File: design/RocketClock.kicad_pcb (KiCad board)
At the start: 2 copper layers, 100 x 100 mm, 98 parts, among them P1 USB_C_Plug_USB2.0, Q1 SS8050, Q2 SS8050, SW1 SW_MEC_5E, U1 TLV75533PDBV, U2 MAX7219, U3 TMP112xxDRL, U4 CH340G, U5 ESP-12F, U6 MAX7219

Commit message: layout mostly done, schematic is done, need to generate new updated pdf
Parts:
- removed the D65 at (428.9, 175.2)
- added BZ1: CBT-09427-SMT-TR, footprints:CUI_CBT-09427-SMT, B.Cu at (191.5, 137.8)
- added C14: 100nF, Capacitor_SMD:C_0402_1005Metric_Pad0.74x0.62mm_HandSolder, B.Cu at (169.8, 70.7)
- added C15: 100nF, Capacitor_SMD:C_0402_1005Metric_Pad0.74x0.62mm_HandSolder, B.Cu at (159.6, 52.9)
- added D2: Green, LED_SMD:LED_0805_2012Metric_Pad1.15x1.40mm_HandSolder, F.Cu at (105.6, 52.2)
- added D66: D_Schottky, Diode_SMD:D_SOD-123, B.Cu at (184.3, 133.7)
- added J1: PROG_CONN, Connector_PinHeader_1.00mm:PinHeader_1x06_P1.00mm_Vertical_SMD_Pin1Left, B.Cu at (176.8, 49.1)
- added J2: Right Output Conn, Package_SO:MagConn, B.Cu at (196.0, 87.9)
- added J3: Left Input Conn, Package_SO:MagConn, B.Cu at (102.5, 87.9)
- added JP1: SolderJumper_2_Bridged, Jumper:SolderJumper-2_P1.3mm_Bridged2Bar_RoundedPad1.0x1.5mm, B.Cu at (169.5, 137.7)
- added Q3: MMBT3906, Package_TO_SOT_SMD:SOT-23, B.Cu at (194.4, 127.4)
- added Q4: BC848W, Package_TO_SOT_SMD:SOT-323_SC-70, B.Cu at (170.2, 131.0)
- added Q5: BC848W, Package_TO_SOT_SMD:SOT-323_SC-70, B.Cu at (167.4, 131.0)
- added Q6: BC848W, Package_TO_SOT_SMD:SOT-323_SC-70, B.Cu at (176.6, 131.0)
- added Q7: BC848W, Package_TO_SOT_SMD:SOT-323_SC-70, B.Cu at (173.4, 131.0)
- added R11: USER, Resistor_SMD:R_0402_1005Metric_Pad0.72x0.64mm_HandSolder, B.Cu at (168.8, 135.3)
- added R12: 2.2k, Resistor_SMD:R_0402_1005Metric_Pad0.72x0.64mm_HandSolder, B.Cu at (167.4, 136.7)
- added R13: 330, Resistor_SMD:R_0402_1005Metric_Pad0.72x0.64mm_HandSolder, B.Cu at (170.2, 134.1)
- added R14: 100, Resistor_SMD:R_0402_1005Metric_Pad0.72x0.64mm_HandSolder, B.Cu at (173.4, 134.1)
- added R15: 330, Resistor_SMD:R_0402_1005Metric_Pad0.72x0.64mm_HandSolder, B.Cu at (168.9, 128.6)
- added R16: 330, Resistor_SMD:R_0402_1005Metric_Pad0.72x0.64mm_HandSolder, B.Cu at (166.2, 128.5)
- added R17: 330, Resistor_SMD:R_0402_1005Metric_Pad0.72x0.64mm_HandSolder, B.Cu at (175.2, 128.4)
- added R18: 330, Resistor_SMD:R_0402_1005Metric_Pad0.72x0.64mm_HandSolder, B.Cu at (172.1, 128.4)
- added R19: 10k, Resistor_SMD:R_0402_1005Metric_Pad0.72x0.64mm_HandSolder, B.Cu at (158.4, 52.9)
- added R20: 10k, Resistor_SMD:R_0402_1005Metric_Pad0.72x0.64mm_HandSolder, B.Cu at (171.6, 52.0)
- added R21: 10k, Resistor_SMD:R_0402_1005Metric_Pad0.72x0.64mm_HandSolder, B.Cu at (182.6, 73.0)
- added R22: 10k, Resistor_SMD:R_0402_1005Metric_Pad0.72x0.64mm_HandSolder, B.Cu at (174.4, 53.3)
- added Y1: 12MHz, Crystal:Crystal_SMD_3225-4Pin_3.2x2.5mm_HandSoldering, B.Cu at (125.9, 59.9)
- C1, C10, C11, C12, C2, C3, C4, C7, C8, C9, D1, Q1, Q2, R1, R10, R7, R8, U1, U2, U4: moved to B.Cu
- C13: value 100nF -> 10uF; moved to B.Cu
- D10, D11, D12, D13, D14, D15, D16, D17, D18, D19, D20, D21, D22, D23, D24, D25, D26, D27, D28, D29, D3, D30, D31, D32, D33, D34, D35, D36, D37, D38, D39, D4, D40, D41, D42, D43, D44, D45, D46, D47, D48, D49, D5, D50, D51, D52, D53, D54, D55, D56, D57, D58, D59, D6, D60, D61, D62, D63, D64, D7, D8, D9: footprint LED_THT:LED_D5.0mm -> LED_SMD:LED_0805_2012Metric_Pad1.15x1.40mm_HandSolder
- D65: renamed from D2; footprint LED_THT:LED_D5.0mm -> LED_SMD:LED_0805_2012Metric_Pad1.15x1.40mm_HandSolder
- P1: value USB_C_Plug_USB2.0 -> INPUT_PWR; moved to B.Cu
- R2: value 14k -> 5.1k; moved to B.Cu
- R3: value 470 -> 5.1k; moved to B.Cu
- R4: value 470 -> 14k; moved to B.Cu
- R5, R6: value 10k -> 470; moved to B.Cu
- R9: value 10k -> 330; moved to B.Cu
- SW1: value SW_MEC_5E -> SW_Push; footprint Button_Switch_SMD:SW_MEC_5GSH9 -> Button_Switch_SMD:SW_Push_1P1T_NO_CK_KSC6xxJ; moved to B.Cu
- U5: value ESP-12F -> ATtiny84A-M; footprint RF_Module:ESP-12E -> Package_DFN_QFN:QFN-20-1EP_4x4mm_P0.5mm_EP2.6x2.6mm; moved to B.Cu
- U6: value MAX7219 -> ESP-12F; footprint Package_SO:SOIC-24W_7.5x15.4mm_P1.27mm -> RF_Module:ESP-12E; moved to B.Cu
- moved D58 323.3 mm to (105.6, 139.8)
- moved D50 317.5 mm to (105.6, 127.2)
- moved D42 312.3 mm to (105.6, 114.8)
- moved D59 310.8 mm to (118.1, 139.8)
- moved R5 309.8 mm to (108.9, 59.0), turned to 180 degrees
- moved D34 307.5 mm to (105.6, 102.2)
- moved D51 305.2 mm to (118.1, 127.2)
- moved D26 303.4 mm to (105.6, 89.8)
- moved D43 300.2 mm to (118.1, 114.8)
- moved P1 300.2 mm to (117.7, 49.5)
- moved D18 299.8 mm to (105.6, 77.2)
- moved U2 299.7 mm to (147.6, 54.2), turned to -90 degrees
- moved D60 298.4 mm to (130.6, 139.8)
- moved R3 297.4 mm to (111.1, 49.1), turned to 90 degrees
- moved C1 297.2 mm to (133.1, 60.5), turned to 90 degrees
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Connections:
- C1 pad 1: +5V -> +3.3V
- C13 pad 1: /MCU/~{RST} -> +3.3V
- C2 pad 1: +3.3V -> +5V
- D1 pad 2: +5V -> /VUSB
- D10 pad 1: /8x8 Module/A -> /8x8 Module/B
- D10 pad 2: /8x8 Module/2 -> /8x8 Module/1
- D12 pad 1: /8x8 Module/C -> /8x8 Module/B
- D12 pad 2: /8x8 Module/2 -> /8x8 Module/3
- D13 pad 1: /8x8 Module/D -> /8x8 Module/B
- D13 pad 2: /8x8 Module/2 -> /8x8 Module/4
- D14 pad 1: /8x8 Module/E -> /8x8 Module/B
- D14 pad 2: /8x8 Module/2 -> /8x8 Module/5
- D15 pad 1: /8x8 Module/F -> /8x8 Module/B
- D15 pad 2: /8x8 Module/2 -> /8x8 Module/6
- D16 pad 1: /8x8 Module/G -> /8x8 Module/B
- D16 pad 2: /8x8 Module/2 -> /8x8 Module/7
- D17 pad 1: /8x8 Module/H -> /8x8 Module/B
- D17 pad 2: /8x8 Module/2 -> /8x8 Module/8
- D18 pad 1: /8x8 Module/A -> /8x8 Module/C
- D18 pad 2: /8x8 Module/3 -> /8x8 Module/1
- D19 pad 1: /8x8 Module/B -> /8x8 Module/C
- D19 pad 2: /8x8 Module/3 -> /8x8 Module/2
- D21 pad 1: /8x8 Module/D -> /8x8 Module/C
- D21 pad 2: /8x8 Module/3 -> /8x8 Module/4
- D22 pad 1: /8x8 Module/E -> /8x8 Module/C
- D22 pad 2: /8x8 Module/3 -> /8x8 Module/5
- D23 pad 1: /8x8 Module/F -> /8x8 Module/C
- D23 pad 2: /8x8 Module/3 -> /8x8 Module/6
- D24 pad 1: /8x8 Module/G -> /8x8 Module/C
- D24 pad 2: /8x8 Module/3 -> /8x8 Module/7
- D25 pad 1: /8x8 Module/H -> /8x8 Module/C
- D25 pad 2: /8x8 Module/3 -> /8x8 Module/8
- D26 pad 1: /8x8 Module/A -> /8x8 Module/D
- D26 pad 2: /8x8 Module/4 -> /8x8 Module/1
- D27 pad 1: /8x8 Module/B -> /8x8 Module/D
- D27 pad 2: /8x8 Module/4 -> /8x8 Module/2
- D28 pad 1: /8x8 Module/C -> /8x8 Module/D
- D28 pad 2: /8x8 Module/4 -> /8x8 Module/3
- D3 pad 1: /8x8 Module/B -> /8x8 Module/A
- D3 pad 2: /8x8 Module/1 -> /8x8 Module/2
- D30 pad 1: /8x8 Module/E -> /8x8 Module/D
- D30 pad 2: /8x8 Module/4 -> /8x8 Module/5
- D31 pad 1: /8x8 Module/F -> /8x8 Module/D
- D31 pad 2: /8x8 Module/4 -> /8x8 Module/6
- D32 pad 1: /8x8 Module/G -> /8x8 Module/D
- D32 pad 2: /8x8 Module/4 -> /8x8 Module/7
- D33 pad 1: /8x8 Module/H -> /8x8 Module/D
- D33 pad 2: /8x8 Module/4 -> /8x8 Module/8
- D34 pad 1: /8x8 Module/A -> /8x8 Module/E
- D34 pad 2: /8x8 Module/5 -> /8x8 Module/1
- D35 pad 1: /8x8 Module/B -> /8x8 Module/E
- D35 pad 2: /8x8 Module/5 -> /8x8 Module/2
- D36 pad 1: /8x8 Module/C -> /8x8 Module/E
- D36 pad 2: /8x8 Module/5 -> /8x8 Module/3
- D37 pad 1: /8x8 Module/D -> /8x8 Module/E
- D37 pad 2: /8x8 Module/5 -> /8x8 Module/4
- D39 pad 1: /8x8 Module/F -> /8x8 Module/E
- D39 pad 2: /8x8 Module/5 -> /8x8 Module/6
- D4 pad 1: /8x8 Module/C -> /8x8 Module/A
- D4 pad 2: /8x8 Module/1 -> /8x8 Module/3
- D40 pad 1: /8x8 Module/G -> /8x8 Module/E
- D40 pad 2: /8x8 Module/5 -> /8x8 Module/7
- D41 pad 1: /8x8 Module/H -> /8x8 Module/E
- D41 pad 2: /8x8 Module/5 -> /8x8 Module/8
- D42 pad 1: /8x8 Module/A -> /8x8 Module/F
- D42 pad 2: /8x8 Module/6 -> /8x8 Module/1
- D43 pad 1: /8x8 Module/B -> /8x8 Module/F
- D43 pad 2: /8x8 Module/6 -> /8x8 Module/2
- D44 pad 1: /8x8 Module/C -> /8x8 Module/F
- D44 pad 2: /8x8 Module/6 -> /8x8 Module/3
- D45 pad 1: /8x8 Module/D -> /8x8 Module/F
- D45 pad 2: /8x8 Module/6 -> /8x8 Module/4
- D46 pad 1: /8x8 Module/E -> /8x8 Module/F
- D46 pad 2: /8x8 Module/6 -> /8x8 Module/5
- D48 pad 1: /8x8 Module/G -> /8x8 Module/F
- D48 pad 2: /8x8 Module/6 -> /8x8 Module/7
- D49 pad 1: /8x8 Module/H -> /8x8 Module/F
- D49 pad 2: /8x8 Module/6 -> /8x8 Module/8
- D5 pad 1: /8x8 Module/D -> /8x8 Module/A
- D5 pad 2: /8x8 Module/1 -> /8x8 Module/4
- D50 pad 1: /8x8 Module/A -> /8x8 Module/G
- D50 pad 2: /8x8 Module/7 -> /8x8 Module/1
- D51 pad 1: /8x8 Module/B -> /8x8 Module/G
- D51 pad 2: /8x8 Module/7 -> /8x8 Module/2
- D52 pad 1: /8x8 Module/C -> /8x8 Module/G
- D52 pad 2: /8x8 Module/7 -> /8x8 Module/3
- D53 pad 1: /8x8 Module/D -> /8x8 Module/G
- D53 pad 2: /8x8 Module/7 -> /8x8 Module/4
- D54 pad 1: /8x8 Module/E -> /8x8 Module/G
- D54 pad 2: /8x8 Module/7 -> /8x8 Module/5
- D55 pad 1: /8x8 Module/F -> /8x8 Module/G
- D55 pad 2: /8x8 Module/7 -> /8x8 Module/6
- D57 pad 1: /8x8 Module/H -> /8x8 Module/G
- D57 pad 2: /8x8 Module/7 -> /8x8 Module/8
- D58 pad 1: /8x8 Module/A -> /8x8 Module/H
- D58 pad 2: /8x8 Module/8 -> /8x8 Module/1
- D59 pad 1: /8x8 Module/B -> /8x8 Module/H
- D59 pad 2: /8x8 Module/8 -> /8x8 Module/2
- D6 pad 1: /8x8 Module/E -> /8x8 Module/A
- D6 pad 2: /8x8 Module/1 -> /8x8 Module/5
- D60 pad 1: /8x8 Module/C -> /8x8 Module/H
- D60 pad 2: /8x8 Module/8 -> /8x8 Module/3
- D61 pad 1: /8x8 Module/D -> /8x8 Module/H
- D61 pad 2: /8x8 Module/8 -> /8x8 Module/4
- D62 pad 1: /8x8 Module/E -> /8x8 Module/H
- D62 pad 2: /8x8 Module/8 -> /8x8 Module/5
- D63 pad 1: /8x8 Module/F -> /8x8 Module/H
- D63 pad 2: /8x8 Module/8 -> /8x8 Module/6
- D64 pad 1: /8x8 Module/G -> /8x8 Module/H
- D64 pad 2: /8x8 Module/8 -> /8x8 Module/7
- D65 pad 1: /8x8 Module/A -> /8x8 Module/H
- D65 pad 2: /8x8 Module/1 -> /8x8 Module/8
- D7 pad 1: /8x8 Module/F -> /8x8 Module/A
- D7 pad 2: /8x8 Module/1 -> /8x8 Module/6
- D8 pad 1: /8x8 Module/G -> /8x8 Module/A
- D8 pad 2: /8x8 Module/1 -> /8x8 Module/7
- D9 pad 1: /8x8 Module/H -> /8x8 Module/A
- D9 pad 2: /8x8 Module/1 -> /8x8 Module/8
- P1 pad A4: +5V -> /VUSB
- P1 pad A9: +5V -> /VUSB
- P1 pad B4: +5V -> /VUSB
- P1 pad B9: +5V -> /VUSB
- Q1 pad 3: /USB_2_UART/RST -> /MCU/~{RST}
- R1 pad 1: Net-(P1-CC) -> +3.3V
- R1 pad 2: GND -> /buzzer/SCL
- R10 pad 2: /MCU/GPIO0 -> /RESET
- R2 pad 1: +5V -> +3.3V
- R2 pad 2: Net-(U2-ISET) -> /buzzer/SDA
- R3 pad 1: Net-(U4-TXD) -> Net-(P1-CC)
- R3 pad 2: /MCU/RX -> GND
- R4 pad 1: Net-(U4-RXD) -> +5V
- R4 pad 2: /MCU/TX -> Net-(U2-ISET)
- R5 pad 1: Net-(Q2-B) -> Net-(U4-TXD)
- R5 pad 2: /USB_2_UART/RTS -> /MCU/RX
- R6 pad 1: Net-(Q1-B) -> Net-(U4-RXD)
- R6 pad 2: /USB_2_UART/DTR -> /MCU/TX
- R7 pad 1: +3.3V -> Net-(Q1-B)
- R7 pad 2: Net-(U5-EN) -> /USB_2_UART/DTR
- R8 pad 1: +3.3V -> Net-(Q2-B)
- R8 pad 2: /MCU/~{RST} -> /USB_2_UART/RTS
- R9 pad 1: Net-(U5-GPIO15) -> /buzzer/~{buzzer}
- R9 pad 2: GND -> Net-(Q3-B)
- SW1 pad 2: GND -> /MCU/~{RST}
- U2 pad 24: /8x8 Module/DOUT -> /DOUT
- U3 pad 1: /MCU/SCL -> /buzzer/SCL
- U3 pad 6: /MCU/SDA -> /buzzer/SDA
- U4 pad 13: /USB_2_UART/DTS -> /USB_2_UART/DTR
- U5 pad 1: /MCU/~{RST} -> /buzzer/SCL
- U5 pad 11: unconnected-(U5-GPIO9-Pad11) -> /SCK
- U5 pad 12: unconnected-(U5-GPIO10-Pad12) -> /MISO
- U5 pad 13: unconnected-(U5-MOSI-Pad13) -> /RESET
- U5 pad 14: unconnected-(U5-SCLK-Pad14) -> /MOSI
- U5 pad 15: GND -> /~{trigger}
- U5 pad 16: Net-(U5-GPIO15) -> /buzzer/SDA
- U5 pad 18: /MCU/GPIO0 -> unconnected-(U5-NC-Pad18)
- U5 pad 19: /MCU/SDA -> unconnected-(U5-NC-Pad19)
- U5 pad 2: unconnected-(U5-ADC-Pad2) -> /buzzer/VOL_3
- U5 pad 20: /MCU/SCL -> /buzzer/~{buzzer}
- U5 pad 21: /MCU/RX -> GND
- U5 pad 3: Net-(U5-EN) -> /buzzer/VOL_2
- U5 pad 4: unconnected-(U5-GPIO16-Pad4) -> /buzzer/VOL_1
- U5 pad 5: /MCU/Data -> /buzzer/VOL_0
- U5 pad 6: /MCU/CLK -> unconnected-(U5-NC-Pad6)
- U5 pad 7: /MCU/CS -> unconnected-(U5-NC-Pad7)
- U5 pad 8: +3.3V -> GND
- U5 pad 9: unconnected-(U5-CS0-Pad9) -> +3.3V
- U6 pad 1: /MCU/Data -> /MCU/~{RST}
- U6 pad 10: /8x8 Module/6 -> unconnected-(U6-MISO-Pad10)
- U6 pad 11: /8x8 Module/2 -> unconnected-(U6-GPIO9-Pad11)
- U6 pad 12: /MCU/CS -> unconnected-(U6-GPIO10-Pad12)
- U6 pad 13: /MCU/CLK -> unconnected-(U6-MOSI-Pad13)
- U6 pad 14: /8x8 Module/A -> unconnected-(U6-SCLK-Pad14)
- U6 pad 15: /8x8 Module/F -> GND
- U6 pad 16: /8x8 Module/B -> Net-(U6-GPIO15)
- U6 pad 17: /8x8 Module/G -> unconnected-(U6-GPIO2-Pad17)
- U6 pad 18: Net-(U6-ISET) -> /MCU/GPIO0
- U6 pad 19: +5V -> /buzzer/SDA
- U6 pad 2: /8x8 Module/1 -> unconnected-(U6-ADC-Pad2)
- U6 pad 20: /8x8 Module/C -> /buzzer/SCL
- U6 pad 21: /8x8 Module/E -> /MCU/RX
- U6 pad 22: /8x8 Module/H -> /MCU/TX
- U6 pad 3: /8x8 Module/5 -> Net-(U6-EN)
- U6 pad 4: GND -> unconnected-(U6-GPIO16-Pad4)
- U6 pad 5: /8x8 Module/7 -> /MCU/Data
- U6 pad 6: /8x8 Module/3 -> /MCU/CLK
- U6 pad 7: /8x8 Module/4 -> /MCU/CS
- U6 pad 8: /8x8 Module/8 -> +3.3V
- U6 pad 9: GND -> unconnected-(U6-CS0-Pad9)
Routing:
- net /8x8 Module/H: track 0.00 -> 198.1 mm, vias 0 -> 16
- net +3.3V: track 0.00 -> 188.1 mm, vias 0 -> 4
- net /8x8 Module/G: track 0.00 -> 187.3 mm, vias 0 -> 16
- net /8x8 Module/F: track 0.00 -> 173.7 mm, vias 0 -> 15
- net /8x8 Module/E: track 0.00 -> 158.0 mm, vias 0 -> 15
- net /8x8 Module/D: track 0.00 -> 149.0 mm, vias 0 -> 17
- net /8x8 Module/C: track 0.00 -> 131.5 mm, vias 0 -> 15
- net /buzzer/VOL_3: track 0.00 -> 121.8 mm, vias 0 -> 2
- net /8x8 Module/B: track 0.00 -> 121.1 mm, vias 0 -> 15
- net /buzzer/VOL_2: track 0.00 -> 116.8 mm, vias 0 -> 2
- net /buzzer/VOL_0: track 0.00 -> 114.8 mm, vias 0 -> 2
- net /buzzer/VOL_1: track 0.00 -> 112.8 mm
- net /8x8 Module/A: track 0.00 -> 109.4 mm, vias 0 -> 1
- net /buzzer/~{buzzer}: track 0.00 -> 104.2 mm, vias 0 -> 4
- net /8x8 Module/2: track 0.00 -> 90.7 mm
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- added copper zone on B.Cu, net GND
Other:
- outline, holes or cut-outs redrawn

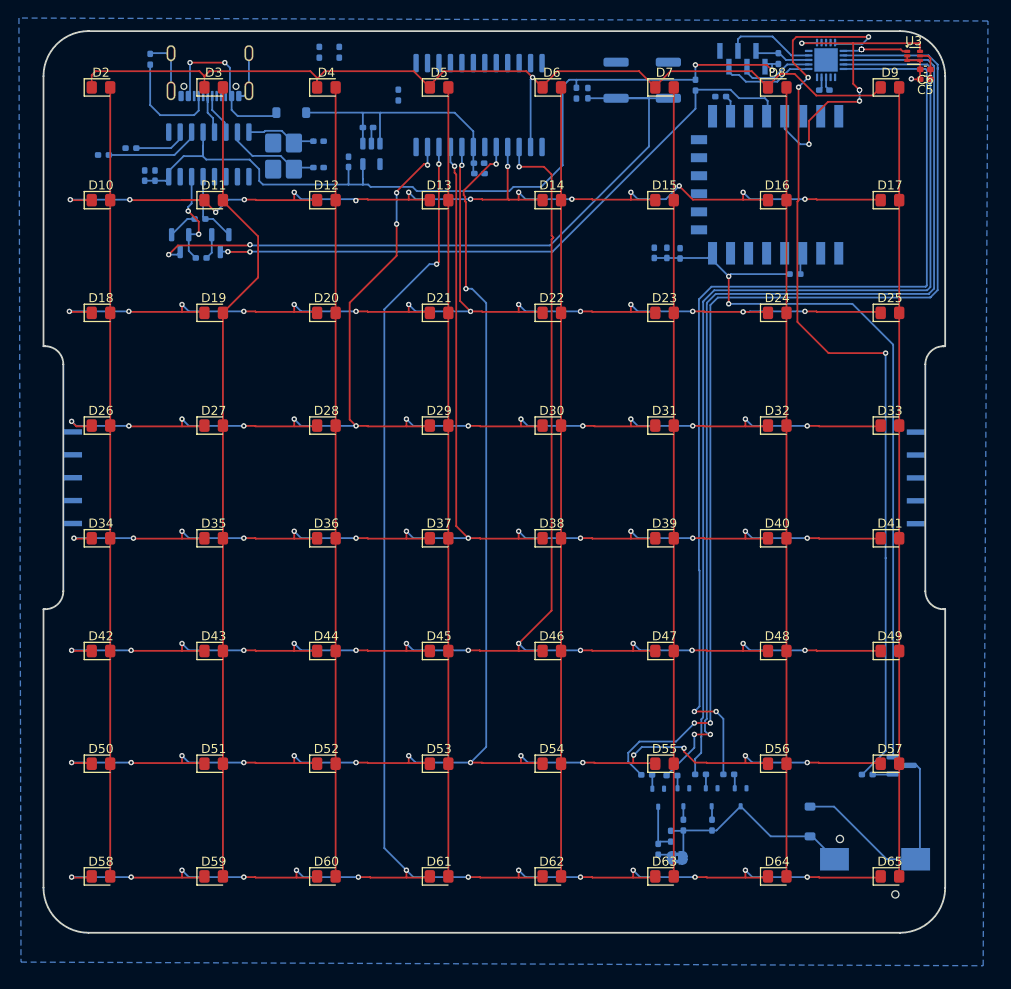
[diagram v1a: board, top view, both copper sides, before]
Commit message: Layout and Schematic Done
Almost ready for first release with tag. DRC etc passing, DFM checks pass on JLCPCB, but I need to go through sourcing components and ensure we have them all available before pushing the button on the orders
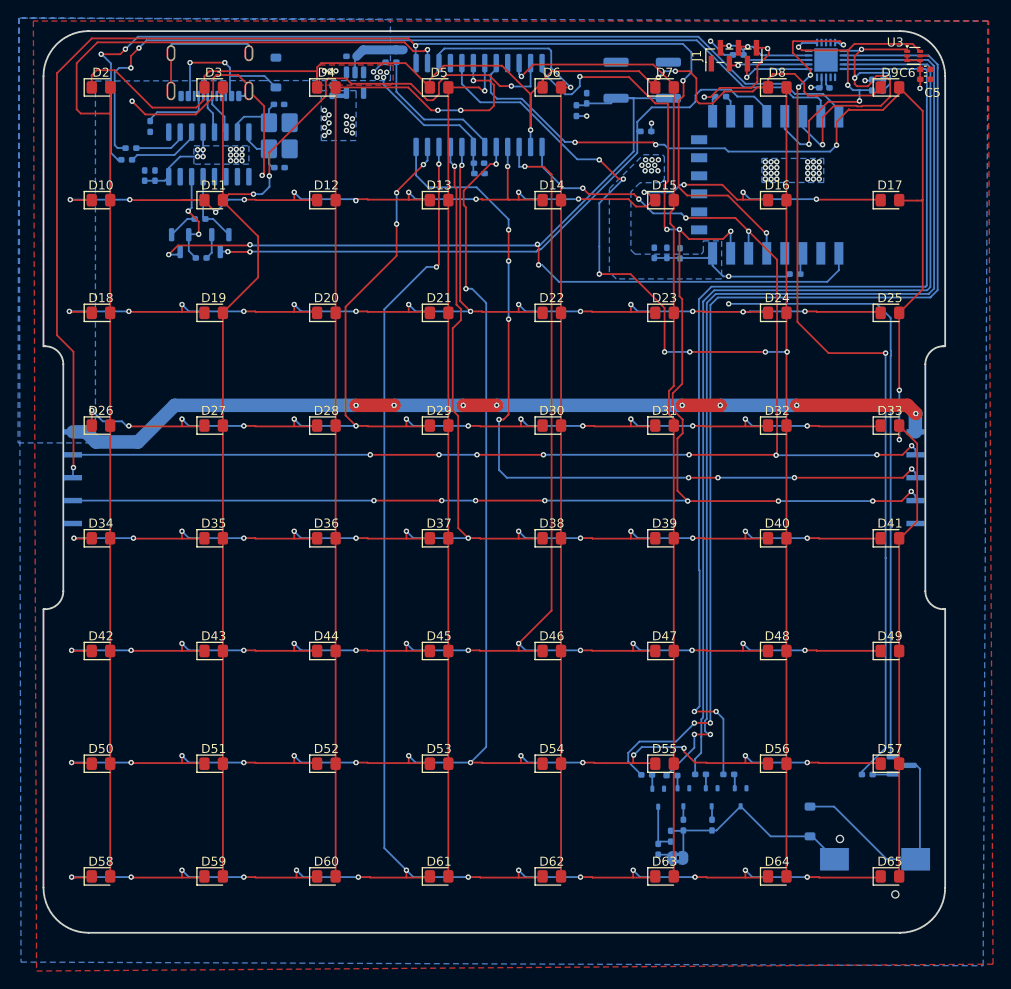
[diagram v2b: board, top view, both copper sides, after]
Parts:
- J1: moved to F.Cu
- moved R2 61.4 mm to (191.1, 52.0)
- moved R1 60.4 mm to (192.4, 52.0)
- moved J2 15.2 mm to (195.9, 103.2), turned to 0 degrees
- moved C9 8.26 mm to (125.4, 54.1)
- moved C1 8.10 mm to (131.3, 52.6)
- moved C2 8.10 mm to (133.4, 48.8)
- moved U1 8.10 mm to (133.8, 51.7)
- moved R20 7.52 mm to (166.1, 57.1), turned to 180 degrees
- moved R3 7.45 mm to (111.1, 56.6), turned to -90 degrees
- moved C10 5.22 mm to (125.4, 61.1)
- moved D1 4.76 mm to (125.0, 50.6), turned to -90 degrees
- moved R10 4.47 mm to (176.3, 48.6), turned to 0 degrees
- moved R4 3.73 mm to (137.8, 49.5), turned to 0 degrees
- moved R6 2.63 mm to (108.5, 60.3)
- moved Y1 2.30 mm to (125.4, 57.6), turned to 90 degrees
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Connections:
- U2 pad 1: /MCU/Data -> /DIN
- U2 pad 12: /MCU/CS -> /~{CS}
- U2 pad 13: /MCU/CLK -> /CLK
- U6 pad 5: /MCU/Data -> /DIN
- U6 pad 6: /MCU/CLK -> /CLK
- U6 pad 7: /MCU/CS -> /~{CS}
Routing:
- net /~{CS}: track 0.00 -> 170.0 mm, vias 0 -> 12
- net /CLK: track 0.00 -> 151.4 mm, vias 0 -> 12
- net /DIN: track 0.00 -> 150.0 mm, vias 0 -> 4
- net /MCU/TX: track 0.00 -> 99.6 mm, vias 0 -> 2
- net /MCU/RX: track 0.00 -> 94.5 mm, vias 0 -> 2
- net /DOUT: track 0.00 -> 91.6 mm, vias 0 -> 8
- net +5V: track 31.1 -> 117.1 mm, vias 0 -> 16
- net +3.3V: track 188.1 -> 109.4 mm, vias 4 -> 66
- net /8x8 Module/8: track 87.5 -> 153.6 mm, vias 0 -> 5
- net /8x8 Module/7: track 87.5 -> 151.0 mm, vias 0 -> 7
- net GND: track 21.6 -> 73.4 mm, vias 1 -> 5
- net /8x8 Module/1: track 87.5 -> 138.4 mm, vias 0 -> 1
- net /8x8 Module/2: track 90.7 -> 139.7 mm, vias 0 -> 3
- net /MCU/~{RST}: track 77.5 -> 115.2 mm, vias 2 -> 4
- net /buzzer/SCL: track 7.27 -> 40.3 mm, vias 4 -> 3
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- added copper zone on B.Cu, net +3.3V
- added copper zone on F.Cu, net +3.3V
- added copper zone on B.Cu, net +5V
- added copper zone on F.Cu, net +5V
